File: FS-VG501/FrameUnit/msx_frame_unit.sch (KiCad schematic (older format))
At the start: 244 parts, among them CN1 Conn_01x02, CN2 Conn_01x10, CN3 Conn_01x04, CN4 Conn_01x10, CN5 Conn_01x10, CN7 Conn_01x06, CN8 Conn_01x06, CN9 Conn_01x02, IC1 74LS245, IC10 74S08, IC11 74LS273, IC12 74LS273, IC13 74LS138, IC14 74LS04, IC15 74LS11, IC16 74S124/74LS629, IC17 74LS153, IC18 74LS153, IC19 74LS153, IC2 74LS244, IC20 74LS08, IC21 SLA6430, IC22 74LS32, IC23 SLA6170, IC24 TC15G008AP, IC24 TC5081AP, IC25 74HC174, IC25 TC15G008AP, IC26 74LS153, IC27 74LS153, IC27 TC15G008AP, IC28 74LS123, IC28 TC15G008AP, IC29 74LS32, IC3 74LS123, IC30 TC15G008AP, IC31 74HC174, IC32 74LS153, IC33 74LS153, IC36 74LS04, IC39 74LS54, IC4 74LS09, IC40 74LS54, IC41 74HC174, IC42 74LS153, IC43 74LS153, IC44 74LS04, IC45 74LS54, IC46 74LS54, IC47 DRAM_4464, IC48 DRAM_4464, IC49 DRAM_4464, IC5 MB40576, IC50 DRAM_4464, IC51 DRAM_4464, IC52 DRAM_4464, IC53 DRAM_4464, IC54 DRAM_4464, IC55 DRAM_4464, IC56 DRAM_4464, IC57 DRAM_4464, IC58 DRAM_4464, IC59 DRAM_4464, IC6 MB40576, IC60 DRAM_4464, IC61 DRAM_4464, IC62 DRAM_4464, IC63 DRAM_4464, IC64 DRAM_4464, IC65 DRAM_4464, IC66 DRAM_4464, IC67 DRAM_4164, IC68 DRAM_4164, IC69 DRAM_4164, IC7 MB40576, IC70 DRAM_4164, IC8 74LS32, IC9 74LS10, Q1 A564_PNP, Q10 C1684_NPN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

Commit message: Add files via upload
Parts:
- IC10: value 74LS08 -> 74S08
- IC16: value 74LS629 -> 74S124/74LS629
- gave numbers to parts that had none: 33
- renumbered IC24 to IC34, IC25 to IC35, IC27 to IC37, IC28 to IC38

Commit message: Add files via upload
added subschema for analog pcb part
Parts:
- added C45: 3300uF/6.3V, symbol Device:CP
- renumbered C45,C48,C49,C53,C60 to C48,C49,C53,C60
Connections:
- net 2G_38 is gone; now on net 2G_3_W: IC57.4 (W)
- net 2G_44 is gone; now on net 2G_4_W: IC58.4 (W)
- net +5V: now also C45.1; no longer C116.1, C54.1
- net +5VA: now also C45.2; no longer IC30.27 (IO), IC34.27 (IO), IC35.27 (IO), IC37.27 (IO), IC38.27 (IO)
- net SLA6430_40: now also IC35.26 (IO)
- net SLA6430_41: now also IC30.27 (IO), IC34.27 (IO), IC35.27 (IO), IC37.27 (IO), IC38.27 (IO)
- net SLA6430_43: now also C54.1
- net SLA6430_70: no longer IC35.57 (IO)
- net at D1.2, IC4.4, IC4.5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: now also C116.1
- new net ': IC35.57 (IO)
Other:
- moved on the sheet: C116, C48,C49,C53,C60, C54
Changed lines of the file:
@@
 $Descr A1 33110 23386
 encoding utf-8
-Sheet 1 1
+Sheet 1 2
 Title ""
 Date ""
@@
 2G_2_W
 Text GLabel 12250 20800 0    50   Input ~ 0
-2G_38
+2G_3_W
 Text GLabel 14150 20800 0    50   Input ~ 0
-2G_44
+2G_4_W
 Text GLabel 16250 19350 0    50   Input ~ 0
 3G_1_W
@@
 $EndComp
 $Comp
-L power:GND #PWR0171
-U 1 1 633BB915
-P 26000 14650
-F 0 "#PWR0171" H 26000 14400 50  0001 C CNN
-F 1 "GND" V 26005 14522 50  0000 R CNN
-F 2 "" H 26000 14650 50  0001 C CNN
-F 3 "" H 26000 14650 50  0001 C CNN
-	1    26000 14650
-	0    1    1    0
-$EndComp
-$Comp
 L power:GND #PWR0172
 U 1 1 63402F97
@@
 $EndComp
 $Comp
-L power:GND #PWR0176
-U 1 1 63570C34
-P 19950 17250
-F 0 "#PWR0176" H 19950 17000 50  0001 C CNN
-F 1 "GND" V 19955 17122 50  0000 R CNN
-F 2 "" H 19950 17250 50  0001 C CNN
-F 3 "" H 19950 17250 50  0001 C CNN
-	1    19950 17250
-	0    1    1    0
-$EndComp
-$Comp
 L power:GND #PWR0177
 U 1 1 635B874E
@@
 $EndComp
 $Comp
-L power:GND #PWR0178
-U 1 1 6360162D
-P 17500 17250
-F 0 "#PWR0178" H 17500 17000 50  0001 C CNN
-F 1 "GND" V 17505 17122 50  0000 R CNN
-F 2 "" H 17500 17250 50  0001 C CNN
-F 3 "" H 17500 17250 50  0001 C CNN
-	1    17500 17250
-	0    1    1    0
-$EndComp
-$Comp
 L power:GND #PWR0180
 U 1 1 63690CD3
@@
 $EndComp
 $Comp
-L power:GND #PWR0184
-U 1 1 637B1AD3
-P 14950 17250
-F 0 "#PWR0184" H 14950 17000 50  0001 C CNN
-F 1 "GND" V 14955 17122 50  0000 R CNN
-F 2 "" H 14950 17250 50  0001 C CNN
-F 3 "" H 14950 17250 50  0001 C CNN
-	1    14950 17250
-	0    1    1    0
-$EndComp
-$Comp
 L power:GND #PWR0187
 U 1 1 638882A4
@@
 $EndComp
 $Comp
-L power:GND #PWR0188
-U 1 1 638CF9BE
-P 12500 17250
-F 0 "#PWR0188" H 12500 17000 50  0001 C CNN
-F 1 "GND" V 12505 17122 50  0000 R CNN
-F 2 "" H 12500 17250 50  0001 C CNN
-F 3 "" H 12500 17250 50  0001 C CNN
-	1    12500 17250
-	0    1    1    0
-$EndComp
-$Comp
 L power:GND #PWR0189
 U 1 1 639171D0
@@
 Text GLabel 14500 12950 3    50   Input ~ 0
 SLA6430_40
-Text GLabel 15050 17150 0    50   Input ~ 0
+Text GLabel 14950 17150 0    50   Input ~ 0
 SLA6430_40
 Text GLabel 17500 17150 0    50   Input ~ 0
@@
 SLA6430_70
 Text GLabel 16100 15350 2    50   Input ~ 0
-SLA6430_70
+'
 Text GLabel 13650 15350 2    50   Input ~ 0
 SLA6430_70
@@
 $EndComp
 Connection ~ 10550 5100
-Wire Wire Line
-	14050 5400 14050 6100
-Wire Wire Line
-	14050 5400 14750 5400
-Wire Wire Line
-	14050 6100 14750 6100
 $Comp
 L agg-kicad:R R85
@@
 	12100 2750 12100 3050
 $Comp
-L Device:CP C45,C48,C49,C53,C60
+L Device:CP C48,C49,C53,C60
 U 1 1 87517B63
-P 15600 2500
-F 0 "C45,C48,C49,C53,C60" H 15718 2546 50  0000 L CNN
-F 1 "2200uF/6.3V" H 15718 2455 50  0000 L CNN
-F 2 "" H 15638 2350 50  0001 C CNN
-F 3 "~" H 15600 2500 50  0001 C CNN
-	1    15600 2500
+P 15450 3300
+F 0 "C48,C49,C53,C60" H 15568 3346 50  0000 L CNN
+F 1 "2200uF/6.3V" H 15568 3255 50  0000 L CNN
+F 2 "" H 15488 3150 50  0001 C CNN
+F 3 "~" H 15450 3300 50  0001 C CNN
+	1    15450 3300
 	1    0    0    -1
 $EndComp
@@
 L Device:CP C54
 U 1 1 875189EC
-P 15600 3300
-F 0 "C54" H 15718 3346 50  0000 L CNN
-F 1 "22uF/6.3V" H 15718 3255 50  0000 L CNN
-F 2 "" H 15638 3150 50  0001 C CNN
-F 3 "~" H 15600 3300 50  0001 C CNN
-	1    15600 3300
+P 14450 13750
+F 0 "C54" H 14568 13796 50  0000 L CNN
+F 1 "22uF/6.3V" H 14568 13705 50  0000 L CNN
+F 2 "" H 14488 13600 50  0001 C CNN
+F 3 "~" H 14450 13750 50  0001 C CNN
+	1    14450 13750
 	1    0    0    -1
 $EndComp
@@
 L Device:CP C116
 U 1 1 87519E5F
-P 15600 2900
-F 0 "C116" H 15718 2946 50  0000 L CNN
-F 1 "220uF/6.3V" H 15718 2855 50  0000 L CNN
-F 2 "" H 15638 2750 50  0001 C CNN
-F 3 "~" H 15600 2900 50  0001 C CNN
-	1    15600 2900
+P 7050 6250
+F 0 "C116" H 7168 6296 50  0000 L CNN
+F 1 "220uF/6.3V" H 7168 6205 50  0000 L CNN
+F 2 "" H 7088 6100 50  0001 C CNN
+F 3 "~" H 7050 6250 50  0001 C CNN
+	1    7050 6250
 	1    0    0    -1
 $EndComp
-Wire Wire Line
-	15600 2650 15350 2650
-Wire Wire Line
-	15350 2650 15350 3050
-Wire Wire Line
-	15350 3050 15600 3050
-Wire Wire Line
-	15350 3050 15350 3450
-Wire Wire Line
-	15350 3450 15600 3450
-Connection ~ 15350 3050
-Wire Wire Line
-	16900 3150 16900 2750
-Wire Wire Line
-	16900 2750 15600 2750
-Wire Wire Line
-	15600 2350 16900 2350
-Wire Wire Line
-	16900 2350 16900 2750
-Connection ~ 16900 2750
 $Comp
 L agg-kicad:GND #PWR0254
@@
 Wire Wire Line
 	15600 3500 15600 3450
-Connection ~ 15600 3450
 $Comp
 L power:+5V #PWR0255
 U 1 1 880ECE56
-P 15600 2350
-F 0 "#PWR0255" H 15600 2200 50  0001 C CNN
-F 1 "+5V" H 15750 2450 50  0000 C CNN
-F 2 "" H 15600 2350 50  0001 C CNN
-F 3 "" H 15600 2350 50  0001 C CNN
-	1    15600 2350
+P 15100 3150
+F 0 "#PWR0255" H 15100 3000 50  0001 C CNN
+F 1 "+5V" H 15250 3250 50  0000 C CNN
+F 2 "" H 15100 3150 50  0001 C CNN
+F 3 "" H 15100 3150 50  0001 C CNN
+	1    15100 3150
 	1    0    0    -1
 $EndComp
@@
 	1    0    0    -1
 $EndComp
-Wire Wire Line
-	14700 3150 15600 3150
-Connection ~ 15350 3450
-Wire Wire Line
-	15350 3450 14700 3450
 Connection ~ 1500 13800
 Wire Wire Line
 	1500 13800 1500 12950
-Connection ~ 15600 2350
-Connection ~ 15600 3150
-Wire Wire Line
-	15600 3150 16900 3150
 $Comp
 L agg-kicad:GND #PWR0256
@@
 	3100 17000 3600 17000
 Wire Wire Line
-	14000 12750 14000 13850
+	14000 12750 14000 13750
 $Comp
 L 74xx:74LS04 IC36
@@
 Text Notes 18050 8950 0    50   ~ 0
 "S0_S1_ENA"
+Text GLabel 12500 17250 0    50   Input ~ 0
+SLA6430_41
+Text GLabel 14950 17250 0    50   Input ~ 0
+SLA6430_41
+Text GLabel 17500 17250 0    50   Input ~ 0
+SLA6430_41
+Text GLabel 19950 17250 0    50   Input ~ 0
+SLA6430_41
+Text GLabel 26000 14650 0    50   Input ~ 0
+SLA6430_41
+Text GLabel 14100 6000 2    50   Input ~ 0
+d0
+Text GLabel 14100 6100 2    50   Input ~ 0
+d1
+Text GLabel 14100 5800 2    50   Input ~ 0
+d2
+Text GLabel 14100 5700 2    50   Input ~ 0
+d3
+Text GLabel 14100 5600 2    50   Input ~ 0
+d4
+Text GLabel 14100 5900 2    50   Input ~ 0
+d5
+Text GLabel 14100 5500 2    50   Input ~ 0
+d6
+Text GLabel 14100 5400 2    50   Input ~ 0
+d7
+Wire Wire Line
+	14350 5400 14350 6100
+Wire Wire Line
+	14350 5400 14750 5400
+Wire Wire Line
+	14350 6100 14750 6100
+Wire Wire Line
+	14700 3150 15100 3150
+Wire Wire Line
+	14150 13900 14150 13750
+Wire Wire Line
+	14150 13750 14000 13750
+Connection ~ 14000 13750
+Wire Wire Line
+	14000 13750 14000 13850
+Wire Wire Line
+	14450 13600 15000 13600
+Wire Wire Line
+	14150 13900 14450 13900
+$Comp
+L power:GND #PWR?
+U 1 1 6241418A
+P 7050 6550
+F 0 "#PWR?" H 7050 6300 50  0001 C CNN
+F 1 "GND" H 7055 6377 50  0000 C CNN
+F 2 "" H 7050 6550 50  0001 C CNN
+F 3 "" H 7050 6550 50  0001 C CNN
+	1    7050 6550
+	1    0    0    -1
+$EndComp
+Wire Wire Line
+	7050 6100 7050 6050
+Connection ~ 7050 6050
+Wire Wire Line
+	7050 6400 7050 6550
+Connection ~ 15450 3450
+Wire Wire Line
+	15450 3450 15600 3450
+Wire Wire Line
+	14700 3450 15450 3450
+Connection ~ 15100 3150
+Wire Wire Line
+	15100 3150 15450 3150
+$Comp
+L Device:CP C45
+U 1 1 630F378B
+P 16450 3300
+F 0 "C45" H 16568 3346 50  0000 L CNN
+F 1 "3300uF/6.3V" H 16568 3255 50  0000 L CNN
+F 2 "" H 16488 3150 50  0001 C CNN
+F 3 "~" H 16450 3300 50  0001 C CNN
+	1    16450 3300
+	1    0    0    -1
+$EndComp
+Wire Wire Line
+	15600 3450 16450 3450
+Connection ~ 15600 3450
+Wire Wire Line
+	16450 3150 15450 3150
+Connection ~ 15450 3150
+$Sheet
+S 2100 8450 2650 2550
+U 60A03B99
+F0 "analog_pcb" 50
+F1 "analog_pcb.sch" 50
+$EndSheet
 $EndSCHEMATC

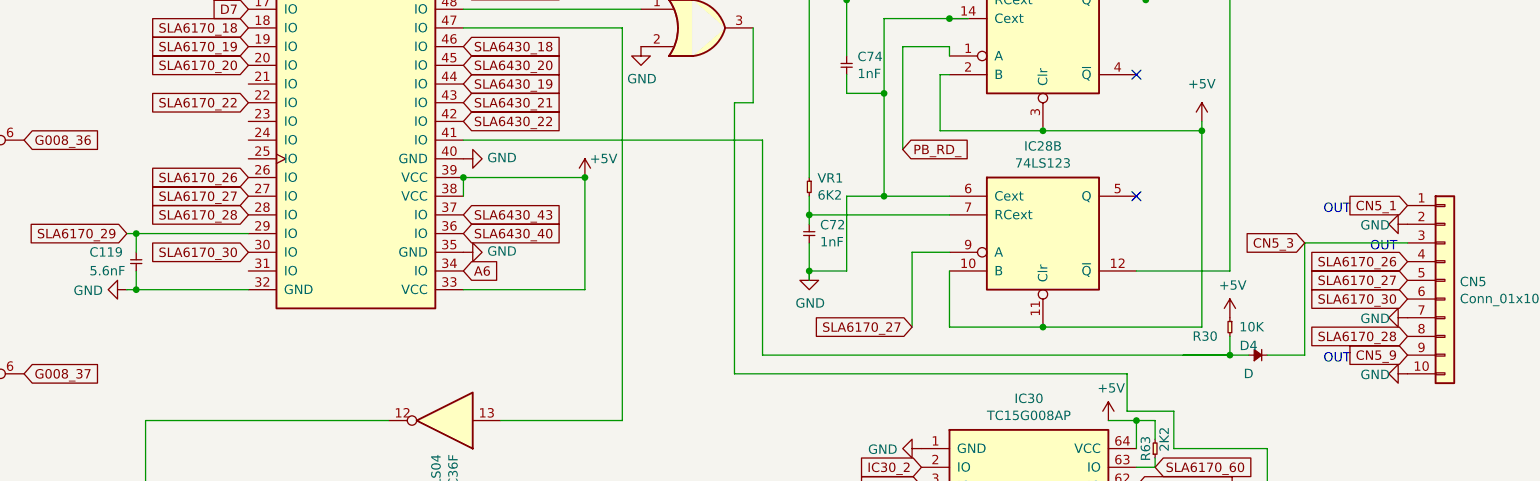
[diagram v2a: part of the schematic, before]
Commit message: added more analog part
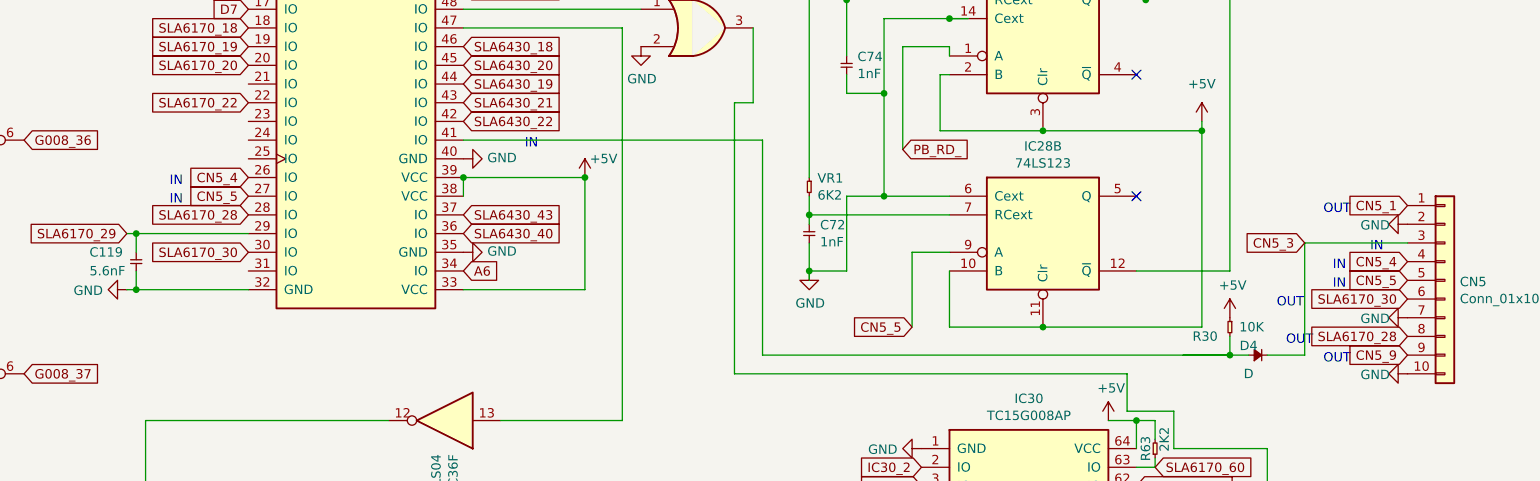
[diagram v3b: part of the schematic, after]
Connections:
- net SLA6170_26 renamed CN5_4
- net SLA6170_27 renamed CN5_5
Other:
- note added: "IN\n"
- note added: "OUT\n"
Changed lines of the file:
@@
 $EndComp
 $Comp
-L power:GND #PWR0201
-U 1 1 64192FA9
-P 28600 10850
-F 0 "#PWR0201" H 28600 10600 50  0001 C CNN
-F 1 "GND" V 28605 10677 50  0000 C CNN
-F 2 "" H 28600 10850 50  0001 C CNN
-F 3 "" H 28600 10850 50  0001 C CNN
-	1    28600 10850
-	0    1    1    0
-$EndComp
-$Comp
 L power:GND #PWR0202
 U 1 1 641D9717
@@
 	17650 20000 16750 20000
 Text GLabel 25950 11400 0    50   Input ~ 0
-SLA6170_27
+CN5_5
 Wire Wire Line
 	25950 11400 25950 11000
@@
 PB_RD_
 Text GLabel 22400 10700 0    50   Input ~ 0
-SLA6170_27
+CN5_5
 Wire Wire Line
 	27150 11100 27650 11100
@@
 	27150 8600 27150 8800
 Text GLabel 28600 11150 0    50   Input ~ 0
-SLA6170_27
+CN5_5
 Text GLabel 22400 11000 0    50   Input ~ 0
 SLA6170_30
@@
 SLA6170_30
 Text GLabel 22400 10600 0    50   Input ~ 0
-SLA6170_26
+CN5_4
 Text GLabel 28600 11050 0    50   Input ~ 0
-SLA6170_26
+CN5_4
 Wire Wire Line
 	21800 11200 22400 11200
@@
 OUT
 Text Notes 28400 11000 0    50   ~ 0
-OUT
+IN\n
 Text Notes 6100 7300 0    50   ~ 0
 OUT
@@
 F1 "analog_pcb.sch" 50
 $EndSheet
+$Comp
+L power:GND #PWR?
+U 1 1 691195A6
+P 28600 10850
+F 0 "#PWR?" H 28600 10600 50  0001 C CNN
+F 1 "GND" V 28605 10677 50  0000 C CNN
+F 2 "" H 28600 10850 50  0001 C CNN
+F 3 "" H 28600 10850 50  0001 C CNN
+	1    28600 10850
+	0    1    1    0
+$EndComp
+Text Notes 28200 11100 0    50   ~ 0
+IN\n
+Text Notes 28200 11200 0    50   ~ 0
+IN\n
+Text Notes 27900 11300 0    50   ~ 0
+OUT\n
+Text Notes 27950 11500 0    50   ~ 0
+OUT\n
+Text Notes 22050 10650 2    50   ~ 0
+IN
+Text Notes 22050 10750 2    50   ~ 0
+IN
+Text Notes 23950 10450 2    50   ~ 0
+IN
 $EndSCHEMATC
